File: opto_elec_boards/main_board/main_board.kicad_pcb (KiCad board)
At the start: 2 copper layers, 216.5 x 68.6 mm, 19 parts, among them J1 IN1_BNC, J2 IN2_BNC, J3 OUT1_BNC, J4 OUT2_BNC, J5 OUT3_BNC, J6 OUT4_BNC, J7 Conn_01x02, J8 Conn_01x02, J9 Conn_01x18, U1 L7805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

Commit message: Update OptoElec Board / Main board
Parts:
- added J10: To Slave Board, Connector_PinSocket_2.54mm:PinSocket_2x10_P2.54mm_Horizontal, F.Cu at (66.5, 58.7)
- added J11: SWITCH_B, Connector_PinSocket_2.54mm:PinSocket_1x03_P2.54mm_Vertical, F.Cu at (177.7, 42.5)
- added J12: SWITCH_C, Connector_PinSocket_2.54mm:PinSocket_1x03_P2.54mm_Vertical, F.Cu at (182.3, 42.5)
- added R1: 8.2k, Resistor_THT:R_Axial_DIN0207_L6.3mm_D2.5mm_P10.16mm_Horizontal, F.Cu at (172.3, 51.9)
- added R2: 8.2k, Resistor_THT:R_Axial_DIN0207_L6.3mm_D2.5mm_P10.16mm_Horizontal, F.Cu at (172.3, 56.0)
- added R3: 8.2k, Resistor_THT:R_Axial_DIN0207_L6.3mm_D2.5mm_P10.16mm_Horizontal, F.Cu at (172.3, 60.0)
- added REF**: MountingHole_4.3mm_M4, MountingHole:MountingHole_4.3mm_M4, F.Cu at (65.0, 45.5)
- added REF**: MountingHole_4.3mm_M4, MountingHole:MountingHole_4.3mm_M4, F.Cu at (65.0, 95.0)
- added REF**: MountingHole_4.3mm_M4, MountingHole:MountingHole_4.3mm_M4, F.Cu at (112.5, 95.0)
- added REF**: MountingHole_4.3mm_M4, MountingHole:MountingHole_4.3mm_M4, F.Cu at (112.5, 45.5)
- added RV1: R_Potentiometer, Connector_PinHeader_2.54mm:PinHeader_1x03_P2.54mm_Vertical, F.Cu at (125.5, 68.5)
- added RV2: R_Potentiometer, Connector_PinHeader_2.54mm:PinHeader_1x03_P2.54mm_Vertical, F.Cu at (108.5, 60.0)
- C3, C4, C5, C6: value 10u -> 10uF; footprint Capacitor_THT:CP_Radial_D8.0mm_P5.00mm -> Capacitor_THT:CP_Radial_D5.0mm_P2.50mm
- J1, J2, J3, J4, J5, J6: footprint Connector_Coaxial:BNC_TEConnectivity_1478204_Vertical -> Connector_PinHeader_2.54mm:PinHeader_1x02_P2.54mm_Vertical
- J7: value Conn_01x02 -> POW_+15V; footprint TerminalBlock_Phoenix:TerminalBlock_Phoenix_MKDS-3-2-5.08_1x02_P5.08mm_Horizontal -> Connector_PinSocket_2.54mm:PinSocket_1x02_P2.54mm_Vertical
- J8: value Conn_01x02 -> POW_-15V; footprint TerminalBlock_Phoenix:TerminalBlock_Phoenix_MKDS-3-2-5.08_1x02_P5.08mm_Horizontal -> Connector_PinSocket_2.54mm:PinSocket_1x02_P2.54mm_Vertical
- J9: value Conn_01x18 -> SWITCH_A; footprint Connector_PinHeader_2.54mm:PinHeader_1x18_P2.54mm_Horizontal -> Connector_PinSocket_2.54mm:PinSocket_1x03_P2.54mm_Vertical
- moved C3 177.7 mm to (86.0, 44.0), turned to 90 degrees
- moved C4 156.2 mm to (86.0, 50.0), turned to -90 degrees
- moved C8 145.2 mm to (93.6, 82.7), turned to 0 degrees
- moved C1 140.3 mm to (123.5, 54.0), turned to 90 degrees
- moved J7 137.8 mm to (119.4, 49.0)
- moved U2 135.7 mm to (127.4, 93.0)
- moved U1 132.6 mm to (93.6, 88.7), turned to 0 degrees
- moved C7 130.6 mm to (74.0, 61.0)
- moved C6 124.3 mm to (128.5, 82.5), turned to 0 degrees
- moved C5 123.9 mm to (95.0, 41.5), turned to -90 degrees
- moved J6 120.3 mm to (88.0, 62.0), turned to 90 degrees
- moved C2 108.0 mm to (136.5, 49.0), turned to -90 degrees
- moved J8 100.4 mm to (141.0, 49.0)
- moved J5 93.8 mm to (88.0, 66.0), turned to 90 degrees
- moved J4 67.7 mm to (88.0, 70.0), turned to 90 degrees
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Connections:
- C4 pad 1: GND -> 5V
- C4 pad 2: -15V -> GND
- C5 pad 1: 5V -> GND
- C5 pad 2: GND -> -15V
- J9 pad 1: 3.3V -> GND
- J9 pad 2: 5V -> SEL1
- J9 pad 3: GND -> 3.3V
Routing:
- net +15V: track 156.8 -> 0.00 mm, vias 1 -> 0
- net IN1: track 128.4 -> 0.00 mm, vias 1 -> 0
- net -15V: track 128.0 -> 0.00 mm, vias 1 -> 0
- net IN2: track 102.7 -> 0.00 mm, vias 1 -> 0
- net 3.3V: track 92.0 -> 0.00 mm, vias 1 -> 0
- net OUT4: track 78.2 -> 0.00 mm, vias 1 -> 0
- net OUT1: track 75.5 -> 0.00 mm, vias 1 -> 0
- net OUT3: track 58.6 -> 0.00 mm, vias 1 -> 0
- net 5V: track 56.4 -> 0.00 mm, vias 1 -> 0
- net OUT2: track 55.1 -> 0.00 mm, vias 1 -> 0
- removed copper zone on B.Cu, net GND
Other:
- board size 216.5 x 68.6 mm -> 63 x 70.5 mm
- net class Default removed
- board text added: "LEnsE / 2026 OPTO-ELEC / Main"
- board text removed: "+15V"
- board text removed: "-15V"
- board text removed: "3.3V"
- board text removed: "5V"
- board text removed: "GND"
- board text removed: "IN1"
- board text removed: "IN2"
- board text removed: "LEnsE / 2021 Alimentation Cartes DEMO"
- board text removed: "LEnsE / 2021 Carte Alim DEMO"
- board text removed: "OUT1"
- board text removed: "OUT2"
- board text removed: "OUT3"
- board text removed: "OUT4"

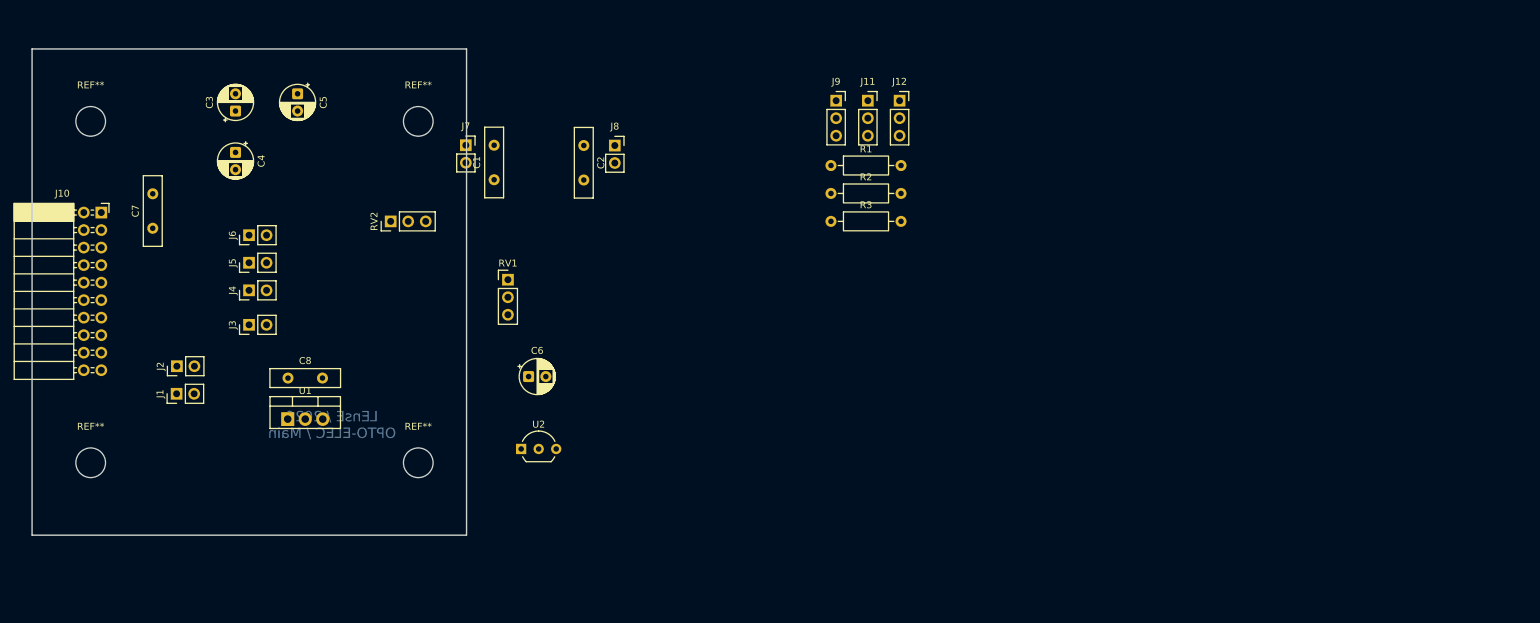
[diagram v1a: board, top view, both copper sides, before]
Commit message: Update Opto new boards / Main and PhotoSlave
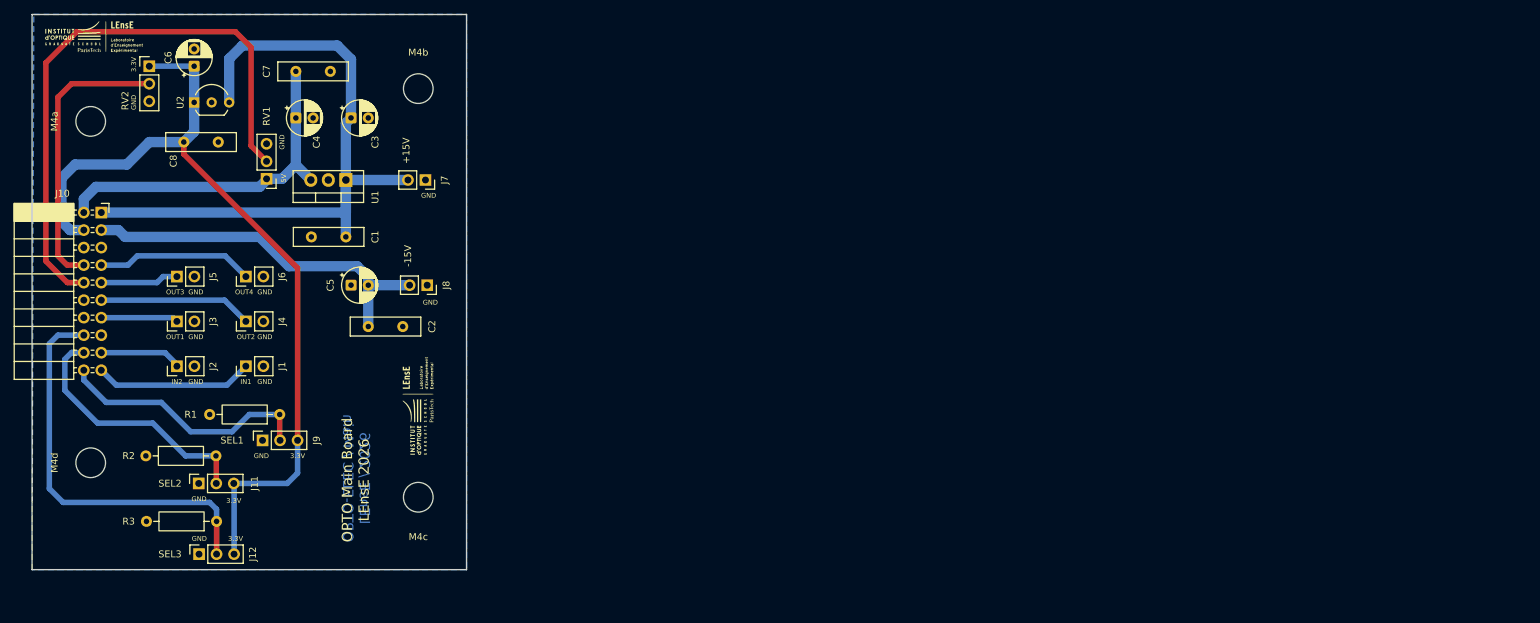
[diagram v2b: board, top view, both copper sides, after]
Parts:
- added G***: LOGO, LEnsE:Logo_Small, F.Cu at (65.5, 33.0)
- added G***: LOGO, LEnsE:Logo_Small, F.Cu at (112.2, 86.8)
- moved J12 121.0 mm to (80.7, 108.2), turned to 90 degrees
- moved J11 111.8 mm to (80.7, 98.0), turned to 90 degrees
- moved R3 99.1 mm to (83.2, 103.5), turned to 180 degrees
- moved R2 97.0 mm to (83.2, 94.0), turned to 180 degrees
- moved J9 96.7 mm to (89.9, 91.8), turned to 90 degrees
- moved R1 87.7 mm to (92.4, 88.0), turned to 180 degrees
- moved U2 69.1 mm to (80.0, 42.8)
- moved C6 66.2 mm to (80.0, 37.5), turned to 90 degrees
- moved RV2 41.6 mm to (73.5, 37.5), turned to 0 degrees
- moved RV1 37.9 mm to (90.5, 53.8), turned to 180 degrees
- moved C8 37.4 mm to (78.5, 48.5)
- moved C2 37.1 mm to (110.2, 75.2), turned to 180 degrees
- moved U1 35.7 mm to (102.0, 54.0), turned to 180 degrees
- moved J8 33.9 mm to (113.8, 69.2), turned to -90 degrees
- moved C7 30.8 mm to (94.8, 38.2), turned to 0 degrees
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- renumbered REF** to M4a, REF** to M4b, REF** to M4c, REF** to M4d
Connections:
- J10 pad 1: 3.3V -> +15V
- J10 pad 14: SEL3 -> GND
- J10 pad 16: SEL2 -> SEL3
- J10 pad 18: SEL1 -> SEL2
- J10 pad 2: +15V -> 5V
- J10 pad 20: GND -> SEL1
- J10 pad 3: 5V -> -15V
- J10 pad 4: -15V -> 3.3V
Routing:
- net 3.3V: track 0.00 -> 123.0 mm
- net +15V: track 0.00 -> 100.1 mm
- net RVAR_5V: track 0.00 -> 85.6 mm
- net SEL3: track 0.00 -> 58.8 mm
- net -15V: track 0.00 -> 54.7 mm
- net 5V: track 0.00 -> 51.5 mm
- net RVAR_3.3V: track 0.00 -> 41.4 mm
- net SEL1: track 0.00 -> 37.8 mm
- net SEL2: track 0.00 -> 37.6 mm
- net IN1: track 0.00 -> 23.0 mm
- net OUT4: track 0.00 -> 22.8 mm
- net OUT2: track 0.00 -> 22.2 mm
- net IN2: track 0.00 -> 11.9 mm
- net OUT3: track 0.00 -> 11.3 mm
- net OUT1: track 0.00 -> 11.2 mm
- added copper zone on B.Cu, net GND
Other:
- board size 63 x 70.5 mm -> 63 x 80.5 mm
- board text added: "+15V"
- board text added: "-15V"
- board text added: "3.3V"
- board text added: "5V"
- board text added: "GND"
- board text added: "IN1"
- board text added: "IN2"
- board text added: "OPTO Main Board LEnsE 2026"
- board text added: "OUT1"
- board text added: "OUT2"
- board text added: "OUT3"
- board text added: "OUT4"
- board text added: "SEL1"
- board text added: "SEL2"
- board text added: "SEL3"
